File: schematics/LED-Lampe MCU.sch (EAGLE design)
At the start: 81 parts, among them IC1 4052D, IC2 TSOP34836, IC3 TSOP34836, IC4 AT45DB161D-SU, IC5 MCP604ST, Q1 CSTCR6M00G53Z, Q2 BSS138, Q3 BSS138

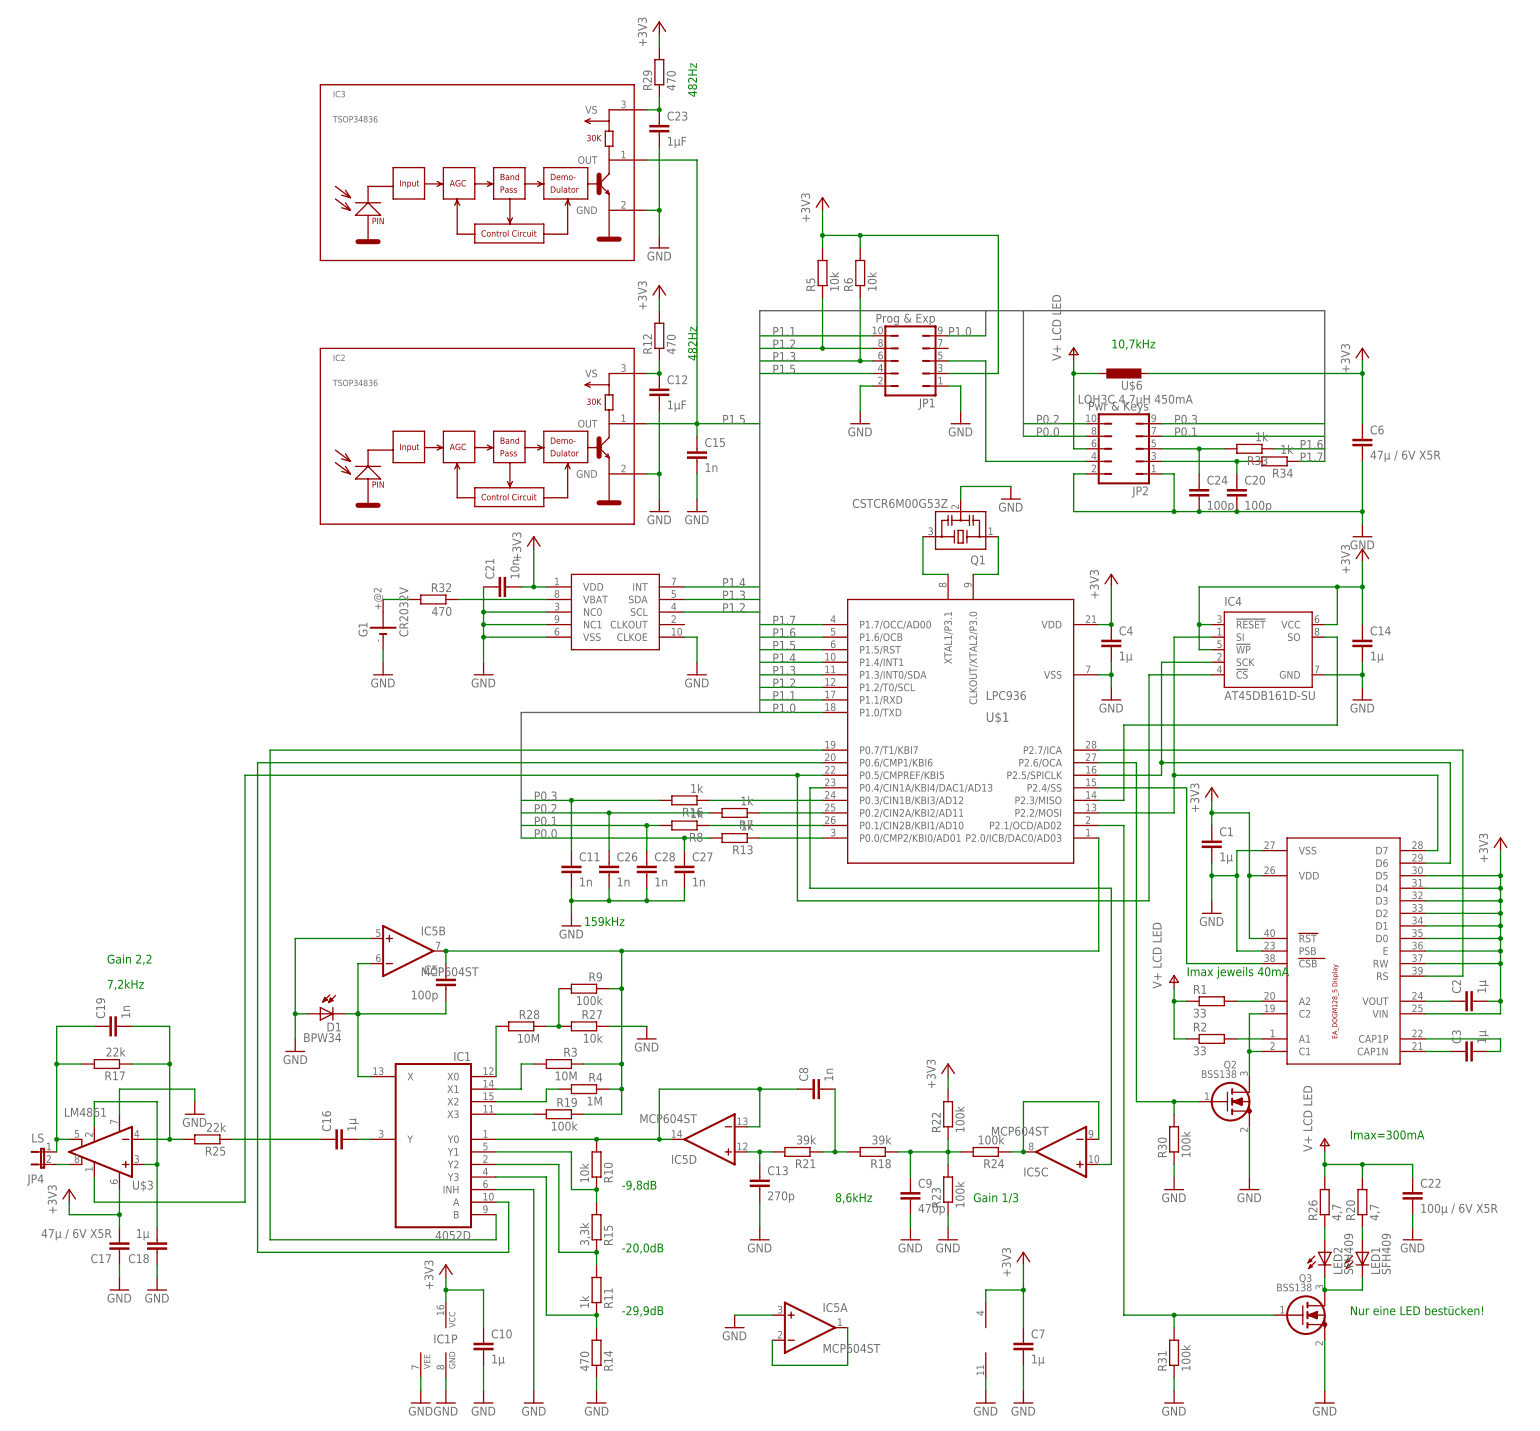
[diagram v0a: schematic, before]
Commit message: - improved placement of IR-LED, IR-Receiver, Photodiode - removed unused devices
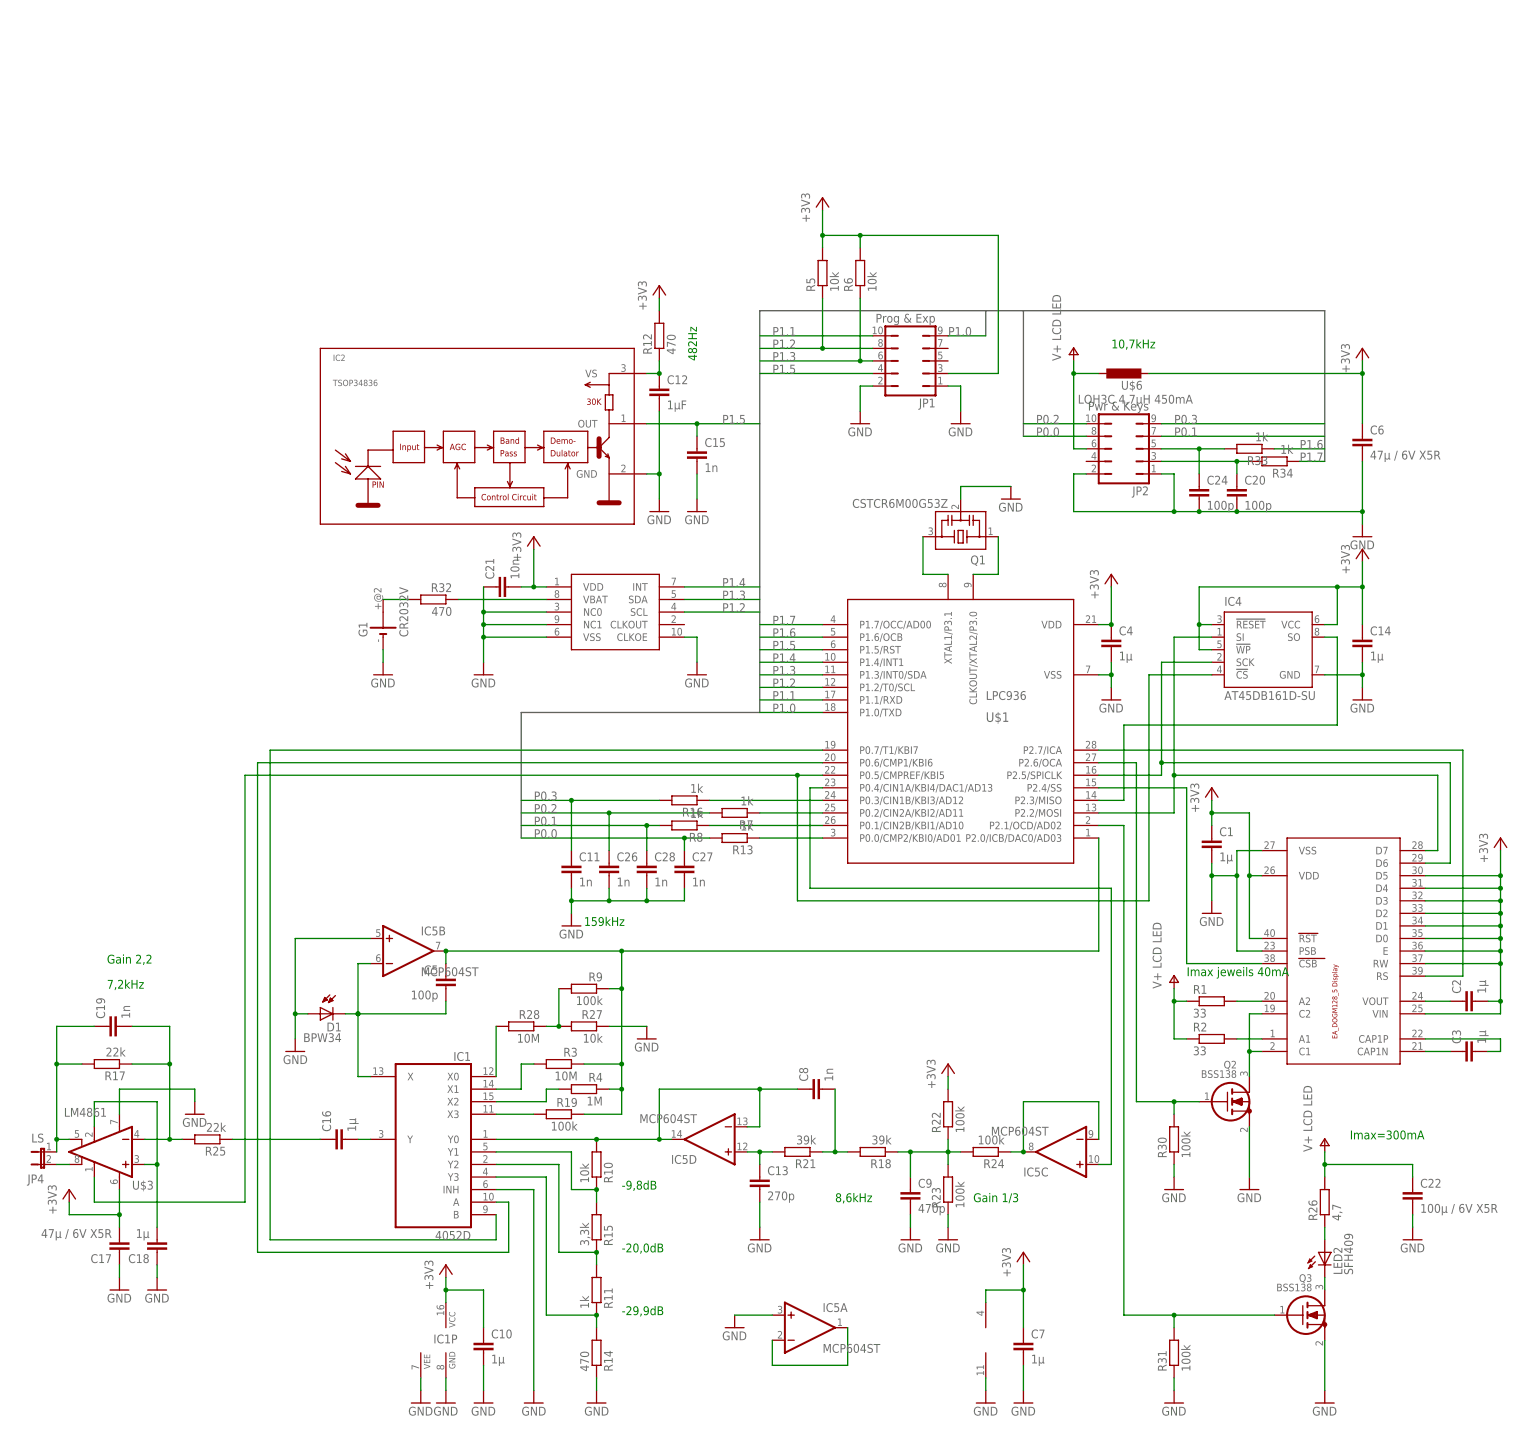
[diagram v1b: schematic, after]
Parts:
- removed C23: 1µF, rcl:C-EUC0805
- removed IC3: TSOP34836, vishay-1:TSOP34836
- removed LED1: SFH409, led:LED3MM
- removed R20: 4,7, rcl:R-EU_R1206
- removed R29: 470, rcl:R-EU_R0805
- R18, R21, R22, R23, R24: device rcl:R-EU_R0805 -> resistor:R-EU_R0805
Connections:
- removed net N$43: JP1.5, JP2.4
- removed net N$48: LED1.A, R20.1
- removed net N$54: C23.1, IC3.VS, R29.1
- net +3V3: no longer R29.2
- net GND: no longer C23.2, IC3.GND
- net N$46: no longer LED1.C
- net P1.5: no longer IC3.OUT
- net V+: no longer R20.2
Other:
- note removed: "Nur eine LED bestücken!"
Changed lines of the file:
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@@
 <?xml version="1.0" encoding="utf-8"?>
 <!DOCTYPE eagle SYSTEM "eagle.dtd">
-<eagle version="6.2">
+<eagle version="6.5.0">
 <drawing>
 <settings>
@@
 <part name="P+2" library="supply1" deviceset="V+" device="" value="V+ LCD LED"/>
 <part name="C13" library="rcl" deviceset="C-EU" device="C0805" value="270p"/>
-<part name="R18" library="rcl" deviceset="R-EU_" device="R0805" value="39k"/>
+<part name="R18" library="resistor" deviceset="R-EU_" device="R0805" value="39k"/>
 <part name="GND14" library="supply1" deviceset="GND" device=""/>
 <part name="JP1" library="jumper" deviceset="JP5Q" device="" value="Prog &amp; Exp"/>
@@
 <part name="GND15" library="supply1" deviceset="GND" device=""/>
 <part name="GND16" library="supply1" deviceset="GND" device=""/>
-<part name="R21" library="rcl" deviceset="R-EU_" device="R0805" value="39k"/>
+<part name="R21" library="resistor" deviceset="R-EU_" device="R0805" value="39k"/>
 <part name="C8" library="rcl" deviceset="C-EU" device="C0805" value="1n"/>
-<part name="R22" library="rcl" deviceset="R-EU_" device="R0805" value="100k"/>
-<part name="R23" library="rcl" deviceset="R-EU_" device="R0805" value="100k"/>
-<part name="R24" library="rcl" deviceset="R-EU_" device="R0805" value="100k"/>
+<part name="R22" library="resistor" deviceset="R-EU_" device="R0805" value="100k"/>
+<part name="R23" library="resistor" deviceset="R-EU_" device="R0805" value="100k"/>
+<part name="R24" library="resistor" deviceset="R-EU_" device="R0805" value="100k"/>
 <part name="GND17" library="supply1" deviceset="GND" device=""/>
 <part name="+3V8" library="supply1" deviceset="+3V3" device=""/>
@@
 <part name="IC5" library="linear" deviceset="MCP604" device="ST"/>
 <part name="GND32" library="supply1" deviceset="GND" device=""/>
-<part name="IC3" library="vishay-1" deviceset="TSOP348*" device="" technology="36"/>
-<part name="R20" library="rcl" deviceset="R-EU_" device="R1206" value="4,7"/>
-<part name="LED1" library="led" deviceset="LED" device="3MM" value="SFH409"/>
-<part name="R29" library="rcl" deviceset="R-EU_" device="R0805" value="470"/>
-<part name="+3V3" library="supply1" deviceset="+3V3" device=""/>
-<part name="GND34" library="supply1" deviceset="GND" device=""/>
-<part name="C23" library="rcl" deviceset="C-EU" device="C0805" value="1µF"/>
 <part name="R30" library="rcl" deviceset="R-EU_" device="R0805" value="100k"/>
 <part name="R31" library="rcl" deviceset="R-EU_" device="R0805" value="100k"/>
@@
 <text x="-93.98" y="-10.16" size="1.778" layer="91">7,2kHz</text>
 <text x="157.48" y="-40.64" size="1.778" layer="91">Imax=300mA</text>
-<text x="25.4" y="170.18" size="1.778" layer="91" rot="R90">482Hz</text>
 <text x="10.16" y="-50.8" size="1.778" layer="91">-9,8dB</text>
 <text x="10.16" y="-63.5" size="1.778" layer="91">-20,0dB</text>
 <text x="10.16" y="-76.2" size="1.778" layer="91">-29,9dB</text>
 <text x="124.46" y="-7.62" size="1.778" layer="91">Imax jeweils 40mA</text>
-<text x="157.48" y="-76.2" size="1.778" layer="91">Nur eine LED bestücken!</text>
 </plain>
 <instances>
@@
 <instance part="IC5" gate="D" x="27.94" y="-40.64" rot="R180"/>
 <instance part="GND32" gate="1" x="33.02" y="-78.74"/>
-<instance part="IC3" gate="G$1" x="-12.7" y="152.4"/>
-<instance part="R20" gate="G$1" x="160.02" y="-53.34" rot="R90"/>
-<instance part="LED1" gate="G$1" x="160.02" y="-63.5"/>
-<instance part="R29" gate="G$1" x="17.78" y="175.26" rot="R90"/>
-<instance part="+3V3" gate="G$1" x="17.78" y="185.42"/>
-<instance part="GND34" gate="1" x="17.78" y="139.7"/>
-<instance part="C23" gate="G$1" x="17.78" y="165.1"/>
 <instance part="R30" gate="G$1" x="121.92" y="-40.64" rot="R90"/>
 <instance part="R31" gate="G$1" x="121.92" y="-83.82" rot="R90"/>
@@
 <pinref part="GND32" gate="1" pin="GND"/>
 <wire x1="40.64" y1="-76.2" x2="33.02" y2="-76.2" width="0.1524" layer="91"/>
-</segment>
-<segment>
-<pinref part="C23" gate="G$1" pin="2"/>
-<pinref part="GND34" gate="1" pin="GND"/>
-<wire x1="17.78" y1="160.02" x2="17.78" y2="147.32" width="0.1524" layer="91"/>
-<pinref part="IC3" gate="G$1" pin="GND"/>
-<wire x1="17.78" y1="147.32" x2="17.78" y2="142.24" width="0.1524" layer="91"/>
-<wire x1="15.24" y1="147.32" x2="17.78" y2="147.32" width="0.1524" layer="91"/>
-<junction x="17.78" y="147.32"/>
 </segment>
 <segment>
@@
 <junction x="58.42" y="142.24"/>
 </segment>
-<segment>
-<pinref part="+3V3" gate="G$1" pin="+3V3"/>
-<pinref part="R29" gate="G$1" pin="2"/>
-<wire x1="17.78" y1="182.88" x2="17.78" y2="180.34" width="0.1524" layer="91"/>
-</segment>
 </net>
 <net name="N$14" class="0">
@@
 <junction x="25.4" y="104.14"/>
 <label x="30.48" y="104.14" size="1.778" layer="95"/>
-<pinref part="IC3" gate="G$1" pin="OUT"/>
-<wire x1="15.24" y1="157.48" x2="25.4" y2="157.48" width="0.1524" layer="91"/>
-<wire x1="25.4" y1="157.48" x2="25.4" y2="104.14" width="0.1524" layer="91"/>
 </segment>
 <segment>
@@
 <wire x1="152.4" y1="-45.72" x2="152.4" y2="-43.18" width="0.1524" layer="91"/>
 <pinref part="C22" gate="G$1" pin="1"/>
-<wire x1="170.18" y1="-45.72" x2="160.02" y2="-45.72" width="0.1524" layer="91"/>
-<wire x1="160.02" y1="-45.72" x2="152.4" y2="-45.72" width="0.1524" layer="91"/>
+<wire x1="170.18" y1="-45.72" x2="152.4" y2="-45.72" width="0.1524" layer="91"/>
 <wire x1="170.18" y1="-48.26" x2="170.18" y2="-45.72" width="0.1524" layer="91"/>
 <pinref part="R26" gate="G$1" pin="2"/>
 <wire x1="152.4" y1="-48.26" x2="152.4" y2="-45.72" width="0.1524" layer="91"/>
 <junction x="152.4" y="-45.72"/>
-<pinref part="R20" gate="G$1" pin="2"/>
-<wire x1="160.02" y1="-48.26" x2="160.02" y2="-45.72" width="0.1524" layer="91"/>
-<junction x="160.02" y="-45.72"/>
 </segment>
 </net>
@@
 </segment>
 </net>
-<net name="N$43" class="0">
-<segment>
-<wire x1="83.82" y1="116.84" x2="83.82" y2="96.52" width="0.1524" layer="91"/>
-<wire x1="83.82" y1="96.52" x2="104.14" y2="96.52" width="0.1524" layer="91"/>
-<pinref part="JP2" gate="B" pin="4"/>
-<pinref part="JP1" gate="B" pin="5"/>
-<wire x1="76.2" y1="116.84" x2="83.82" y2="116.84" width="0.1524" layer="91"/>
-</segment>
-</net>
 <net name="P0.3" class="0">
 <segment>
@@
 <pinref part="LED2" gate="G$1" pin="C"/>
 <wire x1="152.4" y1="-71.12" x2="152.4" y2="-68.58" width="0.1524" layer="91"/>
-<pinref part="LED1" gate="G$1" pin="C"/>
-<wire x1="160.02" y1="-68.58" x2="160.02" y2="-71.12" width="0.1524" layer="91"/>
-<wire x1="160.02" y1="-71.12" x2="152.4" y2="-71.12" width="0.1524" layer="91"/>
-<junction x="152.4" y="-71.12"/>
 </segment>
 </net>
@@
 </segment>
 </net>
-<net name="N$48" class="0">
-<segment>
-<pinref part="LED1" gate="G$1" pin="A"/>
-<pinref part="R20" gate="G$1" pin="1"/>
-<wire x1="160.02" y1="-60.96" x2="160.02" y2="-58.42" width="0.1524" layer="91"/>
-</segment>
-</net>
-<net name="N$54" class="0">
-<segment>
-<pinref part="R29" gate="G$1" pin="1"/>
-<pinref part="C23" gate="G$1" pin="1"/>
-<wire x1="17.78" y1="170.18" x2="17.78" y2="167.64" width="0.1524" layer="91"/>
-<pinref part="IC3" gate="G$1" pin="VS"/>
-<wire x1="15.24" y1="167.64" x2="17.78" y2="167.64" width="0.1524" layer="91"/>
-<junction x="17.78" y="167.64"/>
-</segment>
-</net>
